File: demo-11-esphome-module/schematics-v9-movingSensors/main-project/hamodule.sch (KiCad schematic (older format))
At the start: 63 parts, among them J1 1017505, J2 Conn-ESP-Relays, J3 1017505, J4 Conn-Buttons, J5 Conn_01x02, J6 Conn-Esp-Sensors, J7 Conn-LedIndicators, J8 1017505, J9 Conn_01x02_Male, K1 G5Q-1, K2 G5Q-1, K3 G5Q-1, K4 G5Q-1, U1 ULN2003A, U2 LD1117S33TR_SOT223, U3 HCPL3700, U4 HCPL3700, U5 HCPL3700, U6 HCPL3700

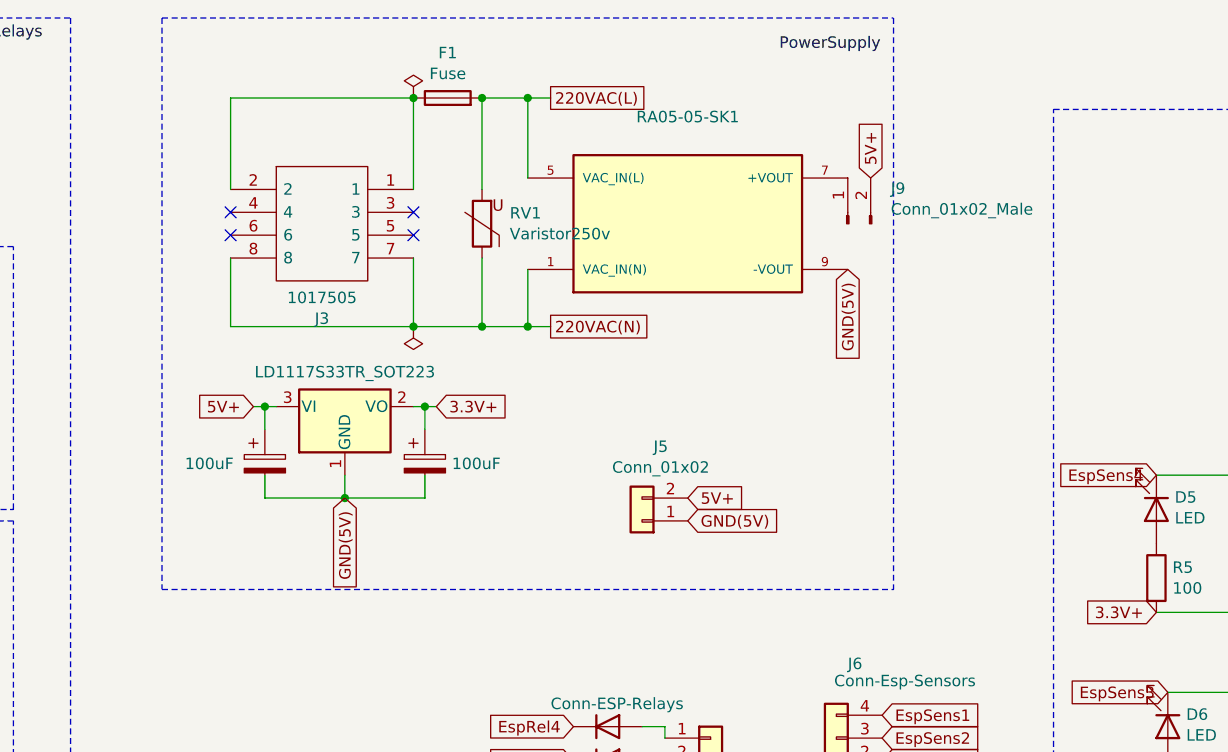
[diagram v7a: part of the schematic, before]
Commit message: sent to jlcpcb! + esp32 init + smaller caps
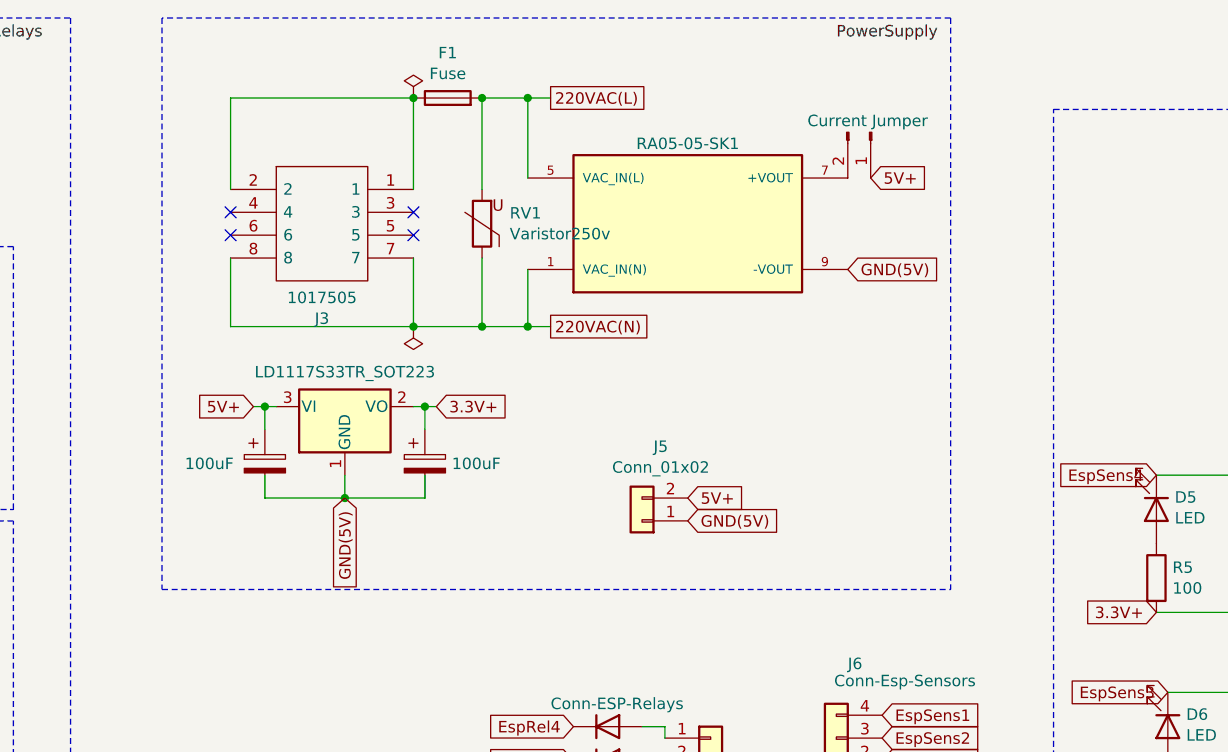
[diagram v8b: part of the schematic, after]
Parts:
- J9: value Conn_01x02_Male -> Current Jumper
- renumbered C1 to 100uF_1, C2 to 100uF_2
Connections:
- net 5V+: now also J9.1 (Pin_1); no longer J9.2 (Pin_2)
- net at RA05-05-SK1.7 (+VOUT): now also J9.2 (Pin_2); no longer J9.1 (Pin_1)
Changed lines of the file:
@@
 	9800 5400 9800 5450
 NoConn ~ 8900 5550
-Wire Notes Line
-	3800 550  7000 550
-Text Label 6500 700  0    50   ~ 0
+Text Label 6750 650  0    50   ~ 0
 PowerSupply
 Text Label 10550 1050 0    50   ~ 0
@@
 Text GLabel 5500 900  2    50   UnSpc ~ 0
 220VAC(L)
-Text GLabel 6800 1650 3    50   Input ~ 0
-GND(5V)
-Text GLabel 6900 1250 1    50   Input ~ 0
-5V+
+Text GLabel 6800 1650 2    50   Input ~ 0
+GND(5V)
 Text GLabel 5500 1900 2    50   UnSpc ~ 0
 220VAC(N)
@@
 NoConn ~ 4100 1400
 NoConn ~ 4100 1500
-$Comp
-L RAC05-05SK_277:RAC05-05SK_277 RA05-05-SK1
-U 1 1 6146ABA1
-P 6100 1450
-F 0 "RA05-05-SK1" H 6100 1917 50  0000 C CNN
-F 1 "RAC05-05SK_277" H 6100 1826 50  0001 C CNN
-F 2 "rac05-05sk:277" H 6100 1450 50  0001 L BNN
-F 3 "" H 6100 1450 50  0001 L BNN
-F 4 "Manufacturer Recommendations" H 6100 1450 50  0001 L BNN "STANDARD"
-F 5 "21.8mm" H 6100 1450 50  0001 L BNN "MAXIMUM_PACKAGE_HEIGHT"
-F 6 "RECOM" H 6100 1450 50  0001 L BNN "MANUFACTURER"
-F 7 "N/A" H 6100 1450 50  0001 L BNN "PARTREV"
-	1    6100 1450
-	1    0    0    -1
-$EndComp
 Text GLabel 4200 2250 0    50   Input ~ 0
 5V+
@@
 GND(5V)
 Wire Notes Line
-	3800 3050 7000 3050
-Wire Notes Line
 	3800 550  3800 3050
 Wire Notes Line
-	7000 550  7000 3050
+	7250 550  7250 3050
 Text GLabel 8200 5500 0    50   Input ~ 0
 EspSens1
@@
 	5800 5200 5750 5200
 $Comp
-L Device:CP C1
+L Device:CP 100uF_1
 U 1 1 6151DFD1
 P 4250 2500
-F 0 "C1" H 4368 2546 50  0001 L CNN
+F 0 "100uF_1" H 4368 2546 50  0001 L CNN
 F 1 "100uF" H 3900 2500 50  0000 L CNN
 F 2 "Capacitor_THT:CP_Radial_D6.3mm_P2.50mm" H 4288 2350 50  0001 C CNN
@@
 $EndComp
 $Comp
-L Device:CP C2
+L Device:CP 100uF_2
 U 1 1 615251C7
 P 4950 2500
-F 0 "C2" H 5068 2546 50  0001 L CNN
+F 0 "100uF_2" H 5068 2546 50  0001 L CNN
 F 1 "100uF" H 5068 2500 50  0000 L CNN
 F 2 "Capacitor_THT:CP_Radial_D6.3mm_P2.50mm" H 4988 2350 50  0001 C CNN
@@
 L Connector:Conn_01x02_Male J9
 U 1 1 6159F81D
-P 6800 1450
-F 0 "J9" V 6954 1262 50  0000 R CNN
-F 1 "Conn_01x02_Male" V 6863 1262 50  0000 R CNN
-F 2 "Connector_PinHeader_2.54mm:PinHeader_1x02_P2.54mm_Vertical" H 6800 1450 50  0001 C CNN
-F 3 "~" H 6800 1450 50  0001 C CNN
-	1    6800 1450
-	0    -1   -1   0
-$EndComp
+P 6900 1050
+F 0 "J9" V 6850 1000 50  0001 R CNN
+F 1 "Current Jumper" V 6850 1300 50  0000 R CNN
+F 2 "Connector_PinHeader_2.54mm:PinHeader_1x02_P2.54mm_Vertical" H 6900 1050 50  0001 C CNN
+F 3 "~" H 6900 1050 50  0001 C CNN
+	1    6900 1050
+	0    1    1    0
+$EndComp
+$Comp
+L RAC05-05SK_277:RAC05-05SK_277 RA05-05-SK1
+U 1 1 6146ABA1
+P 6100 1450
+F 0 "RA05-05-SK1" H 6100 1800 50  0000 C CNN
+F 1 "RAC05-05SK_277" H 6100 1826 50  0001 C CNN
+F 2 "rac05-05sk:277" H 6100 1450 50  0001 L BNN
+F 3 "" H 6100 1450 50  0001 L BNN
+F 4 "Manufacturer Recommendations" H 6100 1450 50  0001 L BNN "STANDARD"
+F 5 "21.8mm" H 6100 1450 50  0001 L BNN "MAXIMUM_PACKAGE_HEIGHT"
+F 6 "RECOM" H 6100 1450 50  0001 L BNN "MANUFACTURER"
+F 7 "N/A" H 6100 1450 50  0001 L BNN "PARTREV"
+	1    6100 1450
+	1    0    0    -1
+$EndComp
+Text GLabel 6900 1250 2    50   Input ~ 0
+5V+
+Wire Notes Line
+	7250 550  3800 550
+Wire Notes Line
+	3800 3050 7250 3050
 $EndSCHEMATC
